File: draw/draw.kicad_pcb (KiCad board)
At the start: 2 copper layers, 35 x 40 mm, 20 parts, among them J1 Input, J2 Ext Conn, U1 INA260, U2 XIAO-ESP32C3

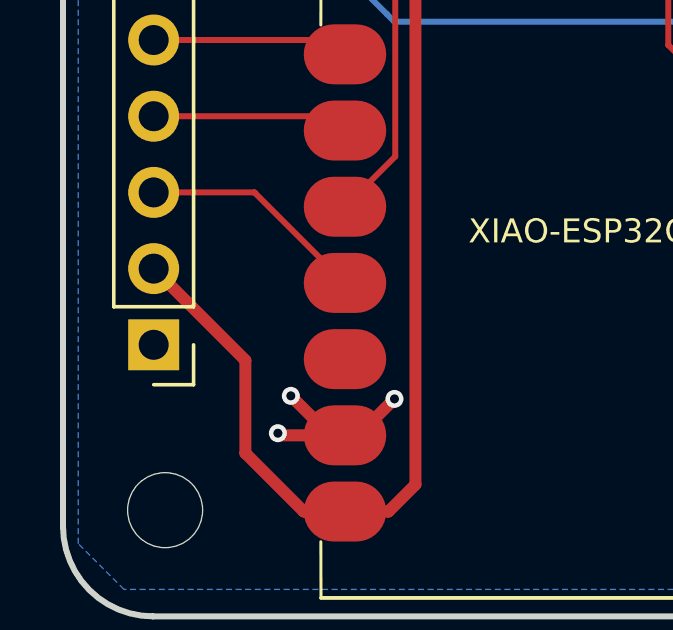
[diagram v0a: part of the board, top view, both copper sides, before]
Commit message: added ibom
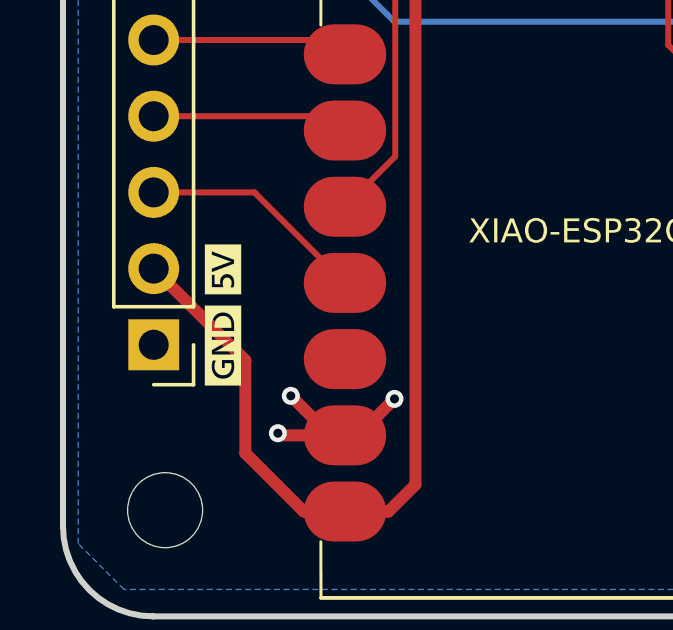
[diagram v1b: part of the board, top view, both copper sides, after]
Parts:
- added kibuzzard-65F4499A: G***, kibuzzard-65F4499A, F.Cu at (106.9, 132.6)
- added kibuzzard-65F449CA: G***, kibuzzard-65F449CA, F.Cu at (106.9, 130.0)
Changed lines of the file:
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@@
+		)
+	)
+	(footprint "kibuzzard-65F449CA"
+		(layer "F.Cu")
+		(at 106.934 130.048 90)
+		(descr "Generated with KiBuzzard")
+		(tags "kb_params=eyJBbGlnbm1lbnRDaG9pY2UiOiAiQ2VudGVyIiwgIkNhcExlZnRDaG9pY2UiOiAiWyIsICJDYXBSaWdodENob2ljZSI6ICJdIiwgIkZvbnRDb21ib0JveCI6ICJGcnV0aWdlciIsICJIZWlnaHRDdHJsIjogIjAuNyIsICJMYXllckNvbWJvQm94IjogIkYuU2lsa1MiLCAiTXVsdGlMaW5lVGV4dCI6ICI1ViIsICJQYWRkaW5nQm90dG9tQ3RybCI6ICI1IiwgIlBhZGRpbmdMZWZ0Q3RybCI6ICI1IiwgIlBhZGRpbmdSaWdodEN0cmwiOiAiNSIsICJQYWRkaW5nVG9wQ3RybCI6ICI1IiwgIldpZHRoQ3RybCI6ICIifQ==")
+		(property "Reference" "kibuzzard-65F449CA"
+			(at 0 -3.653906 90)
+			(layer "F.SilkS")
+			(hide yes)
+			(effects
+				(font
+					(size 0.0254 0.0254)
+				)
+			)
+		)
+		(property "Value" "G***"
+			(at 0 3.653906 90)
+			(layer "F.SilkS")
+			(hide yes)
+			(effects
+				(font
+					(size 0.0254 0.0254)
+				)
+			)
+		)
+		(property "Footprint" ""
+			(at 0 0 90)
+			(unlocked yes)
+			(layer "F.Fab")
+			(hide yes)
+			(effects
+				(font
+					(size 1.27 1.27)
+				)
+			)
+		)
+		(property "Datasheet" ""
+			(at 0 0 90)
+			(unlocked yes)
+			(layer "F.Fab")
+			(hide yes)
+			(effects
+				(font
+					(size 1.27 1.27)
+				)
+			)
+		)
+		(property "Description" ""
+			(at 0 0 90)
+			(unlocked yes)
+			(layer "F.Fab")
+			(hide yes)
+			(effects
+				(font
+					(size 1.27 1.27)
+				)
+			)
+		)
+		(attr board_only exclude_from_pos_files exclude_from_bom)
+		(fp_poly
+			(pts
+				(xy -0.601204 -0.605906) (xy -0.832714 -0.605906) (xy -0.832714 0.605906) (xy -0.601204 0.605906)
+				(xy -0.446562 0.605906) (xy -0.446562 0.374396) (xy -0.501093 0.371683) (xy -0.550199 0.363544)
+				(xy -0.601204 0.348893) (xy -0.597948 0.251225) (xy -0.545316 0.271573) (xy -0.49621 0.284052) (xy -0.447647 0.288122)
+				(xy -0.398609 0.283374) (xy -0.355676 0.269131) (xy -0.293548 0.215413) (xy -0.271301 0.137821)
+				(xy -0.284324 0.075964) (xy -0.322306 0.028215) (xy -0.38145 -0.001899) (xy -0.456871 -0.011937)
+				(xy -0.523883 -0.005562) (xy -0.595778 0.013565) (xy -0.591437 -0.370055) (xy -0.180144 -0.370055)
+				(xy -0.180144 -0.282153) (xy -0.492141 -0.282153) (xy -0.495396 -0.144332) (xy -0.498109 -0.087902)
+				(xy -0.415634 -0.098754) (xy -0.344078 -0.091564) (xy -0.281339 -0.069996) (xy -0.229453 -0.035269)
+				(xy -0.190453 0.011395) (xy -0.166036 0.067961) (xy -0.157897 0.132395) (xy -0.162916 0.184621)
+				(xy -0.177974 0.231691) (xy -0.202526 0.272997) (xy -0.236032 0.307927) (xy -0.27788 0.336074) (xy -0.327461 0.357032)
+				(xy -0.383959 0.370055) (xy -0.446562 0.374396) (xy -0.446562 0.605906) (xy 0.321221 0.605906) (xy 0.321221 0.366799)
+				(xy 0.192081 0.366799) (xy -0.091157 -0.374396) (xy 0.025502 -0.374396) (xy 0.206732 0.114489) (xy 0.234133 0.192353)
+				(xy 0.258821 0.279983) (xy 0.279305 0.203612) (xy 0.309283 0.114489) (xy 0.48997 -0.374396) (xy 0.601204 -0.374396)
+				(xy 0.321221 0.366799) (xy 0.321221 0.605906) (xy 0.601204 0.605906) (xy 0.832714 0.605906) (xy 0.832714 -0.605906)
+				(xy 0.601204 -0.605906) (xy -0.601204 -0.605906)
+			)
+			(stroke
+				(width 0)
+				(type solid)
+			)
+			(fill solid)
+			(layer "F.SilkS")
 		)
 	)
@@
 		)
 	)
+	(footprint "kibuzzard-65F4499A"
+		(layer "F.Cu")
+		(at 106.934 132.588 90)
+		(descr "Generated with KiBuzzard")
+		(tags "kb_params=eyJBbGlnbm1lbnRDaG9pY2UiOiAiQ2VudGVyIiwgIkNhcExlZnRDaG9pY2UiOiAiWyIsICJDYXBSaWdodENob2ljZSI6ICJdIiwgIkZvbnRDb21ib0JveCI6ICJGcnV0aWdlciIsICJIZWlnaHRDdHJsIjogIjAuNyIsICJMYXllckNvbWJvQm94IjogIkYuU2lsa1MiLCAiTXVsdGlMaW5lVGV4dCI6ICJHTkQiLCAiUGFkZGluZ0JvdHRvbUN0cmwiOiAiNSIsICJQYWRkaW5nTGVmdEN0cmwiOiAiNSIsICJQYWRkaW5nUmlnaHRDdHJsIjogIjUiLCAiUGFkZGluZ1RvcEN0cmwiOiAiNSIsICJXaWR0aEN0cmwiOiAiIn0=")
+		(property "Reference" "kibuzzard-65F4499A"
+			(at 0 -3.654991 90)
+			(layer "F.SilkS")
+			(hide yes)
+			(effects
+				(font
+					(size 0.0254 0.0254)
+				)
+			)
+		)
+		(property "Value" "G***"
+			(at 0 3.654991 90)
+			(layer "F.SilkS")
+			(hide yes)
+			(effects
+				(font
+					(size 0.0254 0.0254)
+				)
+			)
+		)
+		(property "Footprint" ""
+			(at 0 0 90)
+			(unlocked yes)
+			(layer "F.Fab")
+			(hide yes)
+			(effects
+				(font
+					(size 1.27 1.27)
+				)
+			)
+		)
+		(property "Datasheet" ""
+			(at 0 0 90)
+			(unlocked yes)
+			(layer "F.Fab")
+			(hide yes)
+			(effects
+				(font
+					(size 1.27 1.27)
+				)
+			)
+		)
+		(property "Description" ""
+			(at 0 0 90)
+			(unlocked yes)
+			(layer "F.Fab")
+			(hide yes)
+			(effects
+				(font
+					(size 1.27 1.27)
+				)
+			)
+		)
+		(attr board_only exclude_from_pos_files exclude_from_bom)
+		(fp_poly
+			(pts
+				(xy 0.591979 -0.279983) (xy 0.591979 0.279983) (xy 0.64624 0.279983) (xy 0.710674 0.278626) (xy 0.757473 0.274557)
+				(xy 0.83398 0.253395) (xy 0.878948 0.228164) (xy 0.91727 0.194794) (xy 0.948198 0.154099) (xy 0.970987 0.106893)
+				(xy 0.985027 0.054667) (xy 0.989707 -0.001085) (xy 0.977227 -0.086816) (xy 0.941415 -0.162781) (xy 0.885527 -0.222467)
+				(xy 0.813904 -0.260992) (xy 0.750148 -0.275371) (xy 0.705044 -0.27883) (xy 0.647325 -0.279983) (xy 0.591979 -0.279983)
+			)
+			(stroke
+				(width 0)
+				(type solid)
+			)
+			(fill solid)
+			(layer "F.SilkS")
+		)
+		(fp_poly
+			(pts
+				(xy -1.103111 -0.606991) (xy -1.334621 -0.606991) (xy -1.334621 0.606991) (xy -1.103111 0.606991)
+				(xy -0.693989 0.606991) (xy -0.693989 0.375481) (xy -0.782433 0.36897) (xy -0.862195 0.349436) (xy -0.932462 0.317287)
+				(xy -0.99242 0.272929) (xy -1.040508 0.217584) (xy -1.075167 0.152471) (xy -1.096125 0.077999) (xy -1.103111 -0.005426)
+				(xy -1.097172 -0.078949) (xy -1.079357 -0.145417) (xy -1.049665 -0.204832) (xy -1.009753 -0.256229)
+				(xy -0.961281 -0.298642) (xy -0.904247 -0.332073) (xy -0.840491 -0.356188) (xy -0.771852 -0.370658)
+				(xy -0.698329 -0.375481) (xy -0.626646 -0.371562) (xy -0.559182 -0.359806) (xy -0.495939 -0.340212)
+				(xy -0.502993 -0.23766) (xy -0.547486 -0.259228) (xy -0.591979 -0.274014) (xy -0.639186 -0.28256)
+				(xy -0.691818 -0.285409) (xy -0.774701 -0.276524) (xy -0.847545 -0.249868) (xy -0.907706 -0.207071)
+				(xy -0.952539 -0.149758) (xy -0.980415 -0.081119) (xy -0.989707 -0.004341) (xy -0.980279 0.075761)
+				(xy -0.951996 0.146774) (xy -0.906485 0.205646) (xy -0.845375 0.249326) (xy -0.771445 0.276388)
+				(xy -0.687477 0.285409) (xy -0.63905 0.281611) (xy -0.587096 0.270216) (xy -0.587096 0.055345) (xy -0.746078 0.055345)
+				(xy -0.746078 -0.034184) (xy -0.481831 -0.034184) (xy -0.481831 0.341297) (xy -0.536295 0.3571)
+				(xy -0.58791 0.367613) (xy -0.639525 0.373514) (xy -0.693989 0.375481) (xy -0.693989 0.606991) (xy 0.295176 0.606991)
+				(xy 0.295176 0.370055) (xy 0.15844 0.370055) (xy -0.075964 -0.032014) (xy -0.127308 -0.123781) (xy -0.159796 -0.184214)
+				(xy -0.181568 -0.232166) (xy -0.200763 -0.286494) (xy -0.196727 -0.223213) (xy -0.193845 -0.155456)
+				(xy -0.192115 -0.083222) (xy -0.191539 -0.006511) (xy -0.191539 0.370055) (xy -0.297346 0.370055)
+				(xy -0.297346 -0.37114) (xy -0.153014 -0.37114) (xy 0.099296 0.065655) (xy 0.144694 0.148311) (xy 0.178878 0.219031)
+				(xy 0.201848 0.277813) (xy 0.196286 0.215685) (xy 0.193709 0.177974) (xy 0.19181 0.092242) (xy 0.190725 0.039067)
+				(xy 0.190453 -0.01465) (xy 0.190453 -0.37114) (xy 0.295176 -0.37114) (xy 0.295176 0.370055) (xy 0.295176 0.606991)
+				(xy 0.654921 0.606991) (xy 0.654921 0.370055) (xy 0.486172 0.370055) (xy 0.486172 -0.37114) (xy 0.639728 -0.37114)
+				(xy 0.710131 -0.369784) (xy 0.763984 -0.365714) (xy 0.835744 -0.352624) (xy 0.902348 -0.327461)
+				(xy 0.961424 -0.291988) (xy 1.010597 -0.247969) (xy 1.0498 -0.195947) (xy 1.078965 -0.136465) (xy 1.097075 -0.070199)
+				(xy 1.103111 0.00217) (xy 1.098702 0.061178) (xy 1.085476 0.117745) (xy 1.064247 0.170309) (xy 1.035828 0.217312)
+				(xy 1.000288 0.258686) (xy 0.957693 0.294362) (xy 0.908995 0.323595) (xy 0.855142 0.345638) (xy 0.798711 0.360288)
+				(xy 0.736583 0.367613) (xy 0.654921 0.370055) (xy 0.654921 0.606991) (xy 1.103111 0.606991) (xy 1.334621 0.606991)
+				(xy 1.334621 -0.606991) (xy 1.103111 -0.606991) (xy -1.103111 -0.606991)
+			)
+			(stroke
+				(width 0)
+				(type solid)
+			)
+			(fill solid)
+			(layer "F.SilkS")
+		)
+	)
